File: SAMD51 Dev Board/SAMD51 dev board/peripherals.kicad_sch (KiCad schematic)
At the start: 27 parts, among them IC1 MCP1603-330I_MC, IC2 MCP1603-180I_MC, J1 Conn_02x08_Top_Bottom, J2 USB_C_Receptacle_USB2.0_14P, J3 FTSH-105-01-L-DV-007-K

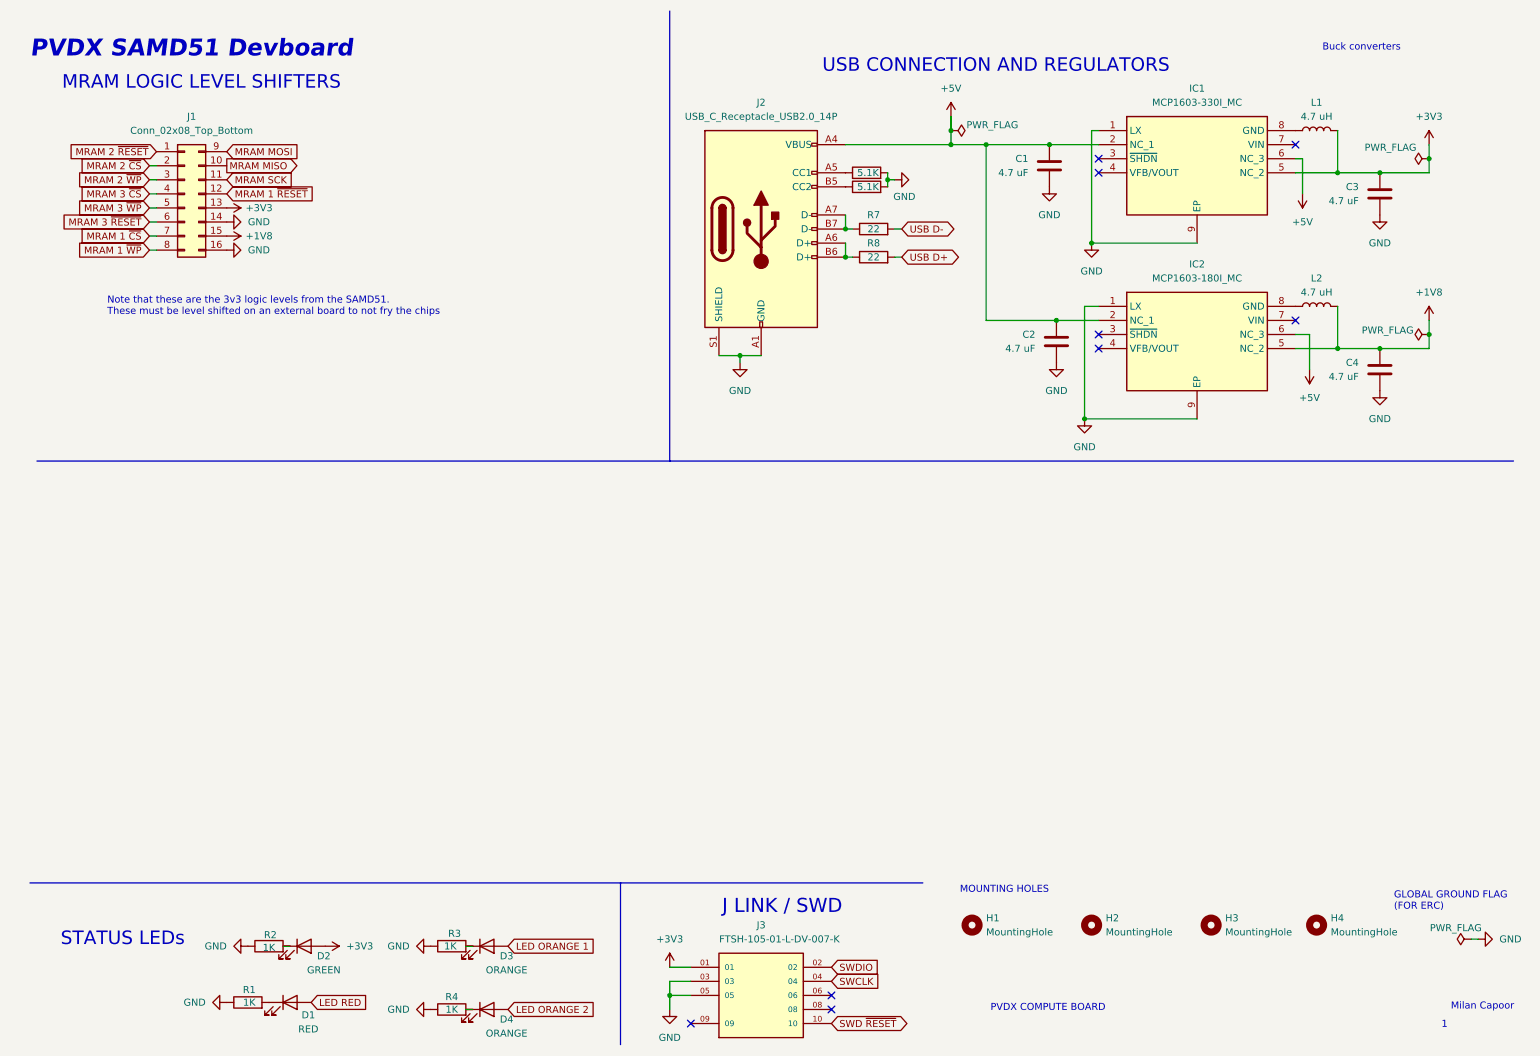
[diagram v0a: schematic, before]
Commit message: routed samd51 breakout
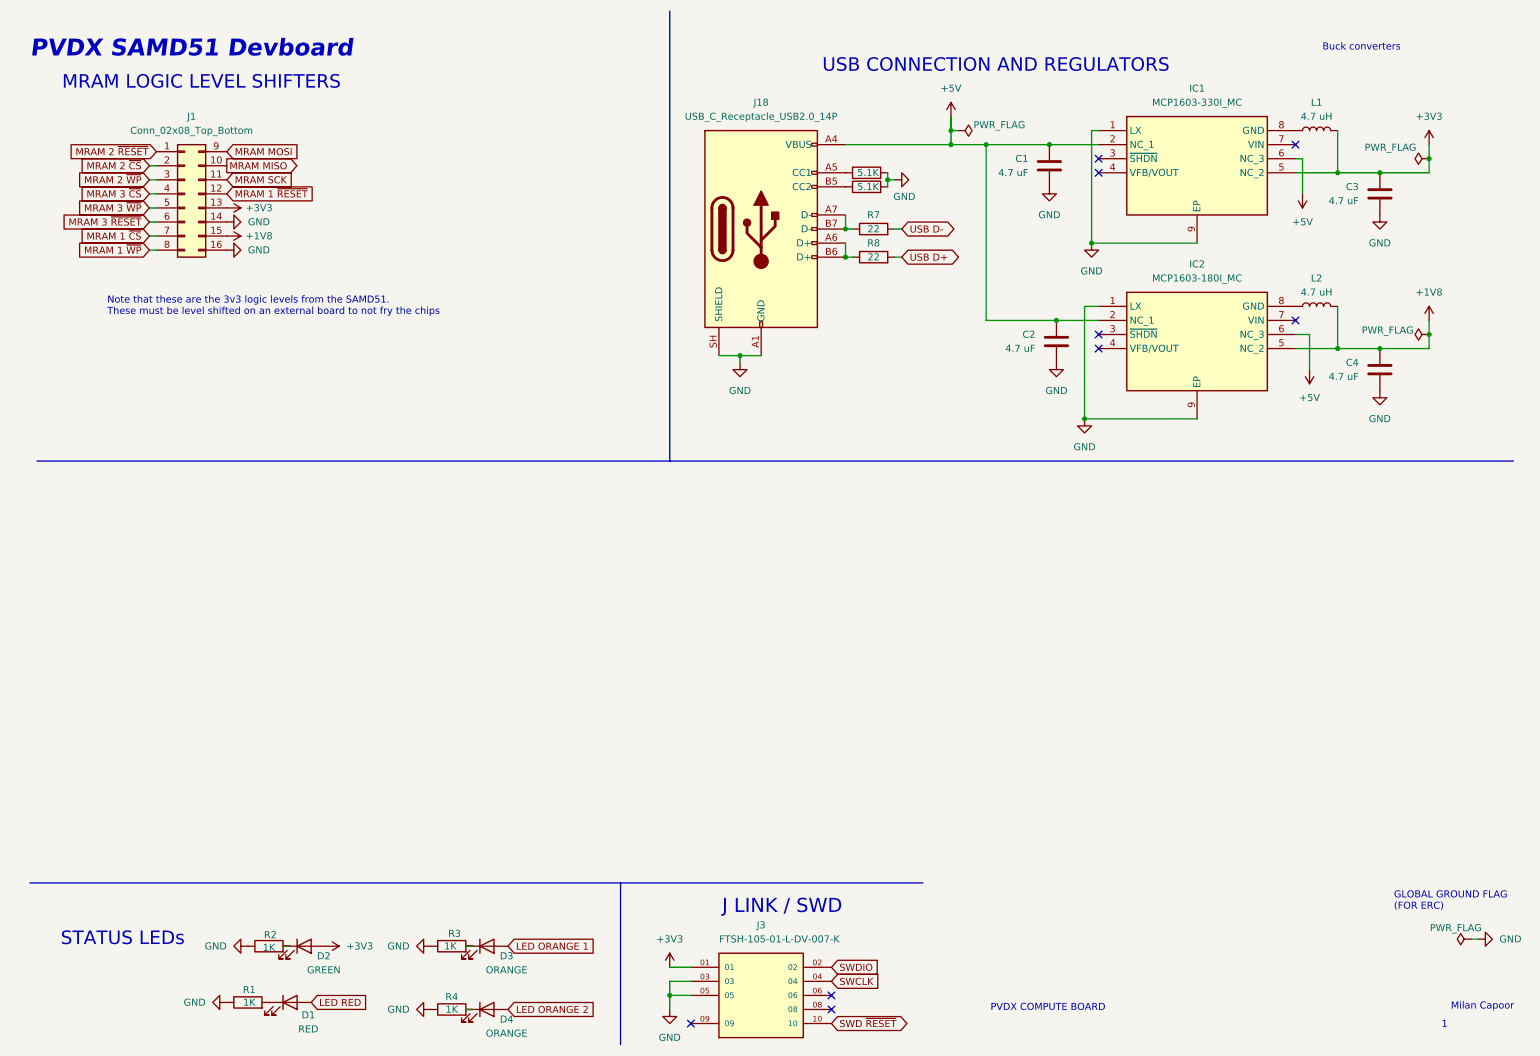
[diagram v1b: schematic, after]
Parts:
- removed H1, H2, H3, H4: MountingHole, MountingHole:MountingHole_2.1mm, symbol Mechanical:MountingHole
- removed J2: USB_C_Receptacle_USB2.0_14P, Connector_USB:USB_C_Receptacle_HCTL_HC-TYPE-C-16P-01A, symbol Connector:USB_C_Receptacle_USB2.0_14P
- added J18: USB_C_Receptacle_USB2.0_14P, Connector_USB:USB_C_Receptacle_G-Switch_GT-USB-7010ASV, symbol Connector:USB_C_Receptacle_USB2.0_14P
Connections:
- net +5V: now also J18.A4 (VBUS), J18.A9 (VBUS), J18.B4 (VBUS), J18.B9 (VBUS)
- net GND: now also J18.A1 (GND), J18.A12 (GND), J18.B1 (GND), J18.B12 (GND), J18.SH (SHIELD)
- net at R8.1: now also J18.A6 (D+), J18.B6 (D+)
- net at R5.1: now also J18.A5 (CC1)
- net at R7.1: now also J18.A7 (D-), J18.B7 (D-)
- net at R6.1: now also J18.B5 (CC2)
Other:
- note removed: "MOUNTING HOLES"
